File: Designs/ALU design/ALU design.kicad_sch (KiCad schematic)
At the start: 41 parts, among them U1 74LS86, U10 74LS08, U11 74LS125, U12 74LS125, U13 74LS32, U14 74LS138, U15 74LS125, U2 74LS86, U3 74LS173, U4 74LS83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

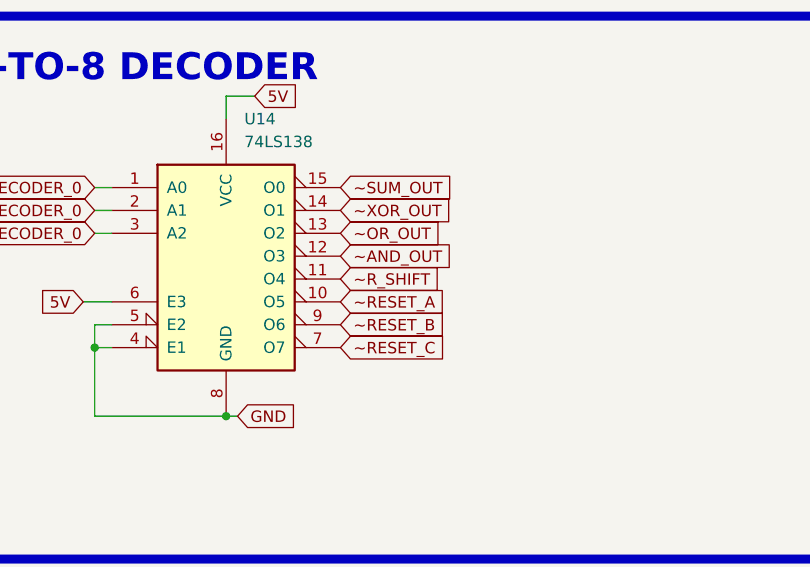
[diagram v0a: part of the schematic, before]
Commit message: Decoder bug is fixed
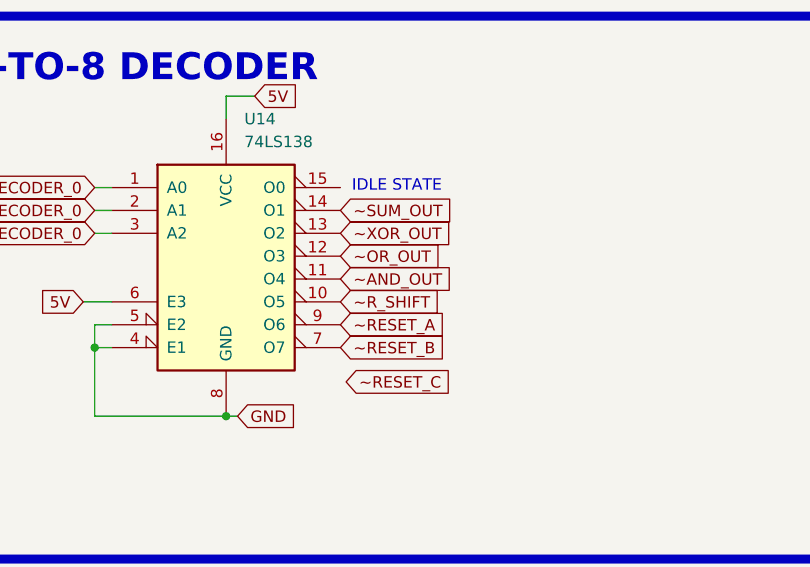
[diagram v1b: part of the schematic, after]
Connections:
- net ~AND_OUT: now also U14.11 (O4); no longer U14.12 (O3)
- net ~OR_OUT: now also U14.12 (O3); no longer U14.13 (O2)
- net ~RESET_A: now also U14.9 (O6); no longer U14.10 (O5)
- net ~RESET_B: now also U14.7 (O7); no longer U14.9 (O6)
- net ~RESET_C: no longer U14.7 (O7)
- net ~R_SHIFT: now also U14.10 (O5); no longer U14.11 (O4)
- net ~SUM_OUT: now also U14.14 (O1); no longer U14.15 (O0)
- net ~XOR_OUT: now also U14.13 (O2); no longer U14.14 (O1)
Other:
- note added: "IDLE STATE"

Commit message: Update ALU design.kicad_sch
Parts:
- added R? (x7): 10k, symbol Device:R
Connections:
- net ALU_DECODER_0: now also R?.2, R?.2, R?.2
- net BUS_0: now also R?.1, R?.2, R?.2, R?.2
- net GND: now also R?.1, R?.1, R?.1, R?.1, R?.1, R?.1, R?.2

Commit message: ALU flags - 3state output buffer to bus
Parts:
- added U? (x10): 74LS125, symbol 74xx:74LS125
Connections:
- net 5V: now also U?.14 (VCC), U?.14 (VCC)
- net BUS_0: now also U?.3, U?.3
- net BUS_1: now also U?.6, U?.6
- net BUS_2: now also U?.8, U?.8
- net BUS_3: now also U?.11, U?.11
- net CARRY_OUT_FLAG_PREVIOUS: now also U?.2
- net GND: now also U?.7 (GND), U?.7 (GND)
- net IS_NEGATIVE_FLAG_PREVIOUS: now also U?.5
- net IS_OVERFLOW_FLAG_PREVIOUS: now also U?.12
- net RESET_A: no longer U1.11
- net RESET_B: no longer U1.8
- net RESET_C: no longer U1.6
- net SUM_0: now also U?.2
- net SUM_1: now also U?.5
- net SUM_2: now also U?.9
- net SUM_3: now also U?.12
- net ~IS_ZERO_FLAG_PREVIOUS: now also U?.9
- net ~SUM_OUT: now also U?.1, U?.10, U?.13, U?.4
- net ~RESET_A: no longer names the net of U1.13
- net ~RESET_A: no longer U14.9 (O6)
- net ~RESET_B: no longer names the net of U1.10
- net ~RESET_B: no longer U14.7 (O7)
- net ~RESET_C: no longer names the net of U1.5
- new net ~FLAGS_OUT: U14.9 (O6), U?.1, U?.10, U?.13, U?.4
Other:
- moved on the sheet: C?, U6, U7
